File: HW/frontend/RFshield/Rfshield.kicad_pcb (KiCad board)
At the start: 4 copper layers, 73 x 50.9 mm, 148 parts, among them P10 TXENABLE, P11 RXENABLE, P12 XTAL2, P13 GCK1, P14 GCK2, P15 SGPIO_CLK, P16 DA0, P17 DA4, P18 DA7, P19 DD0, P2 VAA, P20 DD5, P21 DD9, P22 RSSI, P23 GND, P24 GND, P25 GND, P26 GND, P27 GND, P28 GND, P29 GND, P3 SCL, P30 GND, P31 GND, P32 GND, P33 XCVR_CLKOUT, P37 INTR, P38 CLKIN, P39 CLKOUT, P4 SDA, P5 SSP1_SCK, P6 SSP1_MOSI, P7 SSP1_MISO, P8 CS_XCVR, P9 CS_AD, Q1 MOSFET_P, T1 RX_BALUN, T2 TX_BALUN, U1 MAX2837, U2 MAX5864, X1 GSG-XTAL4PIN

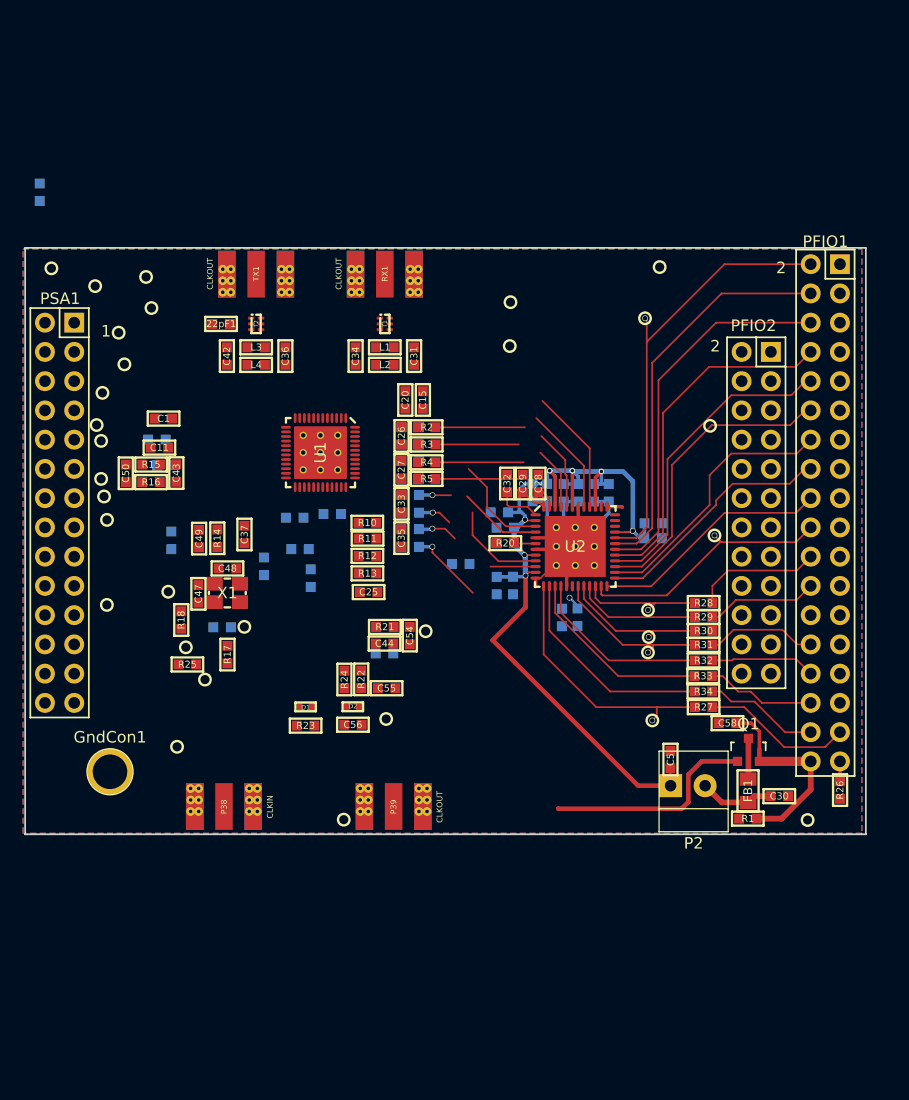
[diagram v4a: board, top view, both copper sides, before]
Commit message: components placed
components placed with reviewed footprints
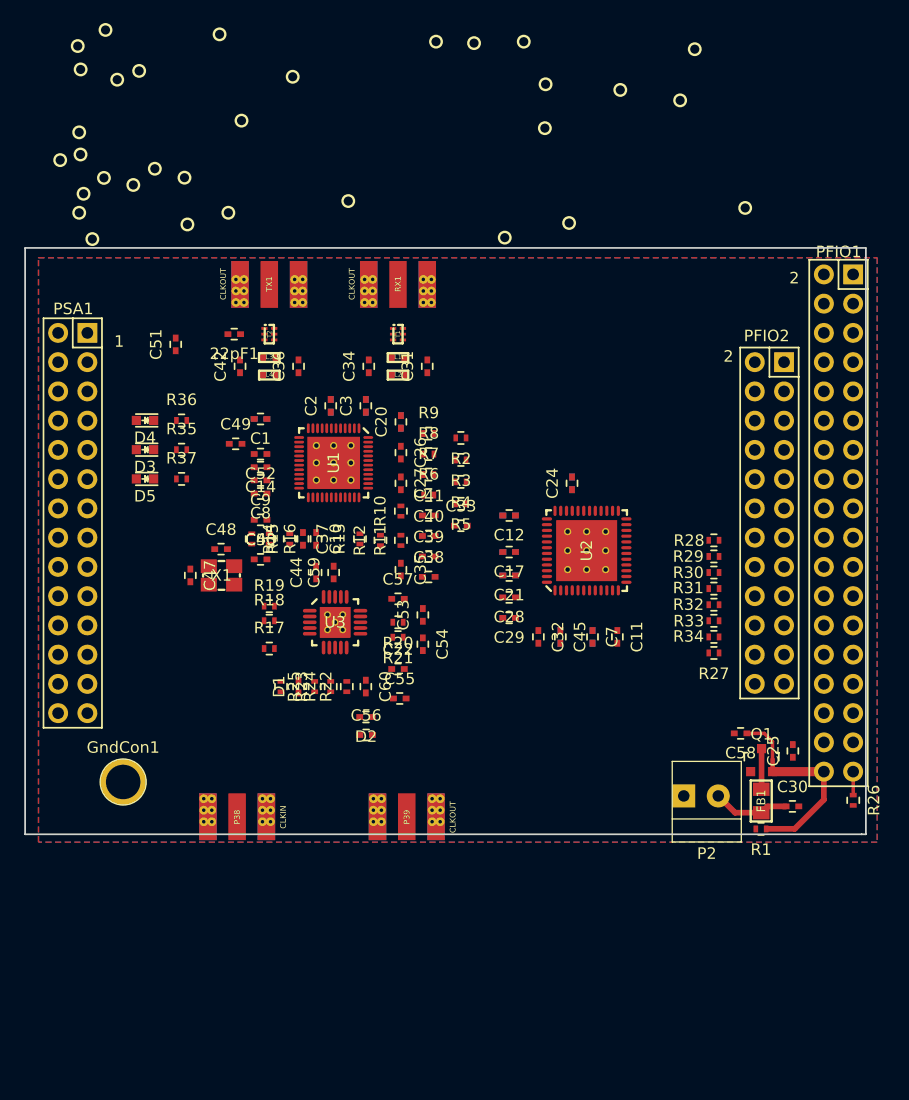
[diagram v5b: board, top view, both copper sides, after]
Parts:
- added C9: 10nF, Capacitors_SMD:C_0402, F.Cu at (39.8, 86.5)
- added D3: LED, LEDs:LED-0603, F.Cu at (29.7, 83.8)
- added D4: LED, LEDs:LED-0603, F.Cu at (29.7, 81.3)
- added D5: LED, LEDs:LED-0603, F.Cu at (29.7, 86.4)
- added R35: 475, Resistors_SMD:R_0402, F.Cu at (32.9, 83.8)
- added R36: 475, Resistors_SMD:R_0402, F.Cu at (32.9, 81.3)
- added R37: 475, Resistors_SMD:R_0402, F.Cu at (32.9, 86.4)
- added U3: SI5351C, hackrf1:GSG-QFN20-4, F.Cu at (46.2, 98.8)
- 22pF1, C1, C11, C13, C16, C18, C19, C20, C23, C25, C26, C27, C28, C29, C30, C31, C32, C33, C34, C35, C36, C37, C4, C42, C43, C44, C46, C47, C48, C49, C50, C54, C55, C56, C58, C6: footprint hackrf1:GSG-0603 -> Capacitors_SMD:C_0402
- C10, C12, C14, C17, C2, C21, C22, C24, C3, C38, C39, C40, C41, C45, C51, C52, C53, C57, C59, C60, C7, C8: footprint hackrf1:GSG-0603 -> Capacitors_SMD:C_0402; moved to F.Cu
- C15, C5: footprint hackrf1:GSG-0603 -> Capacitors_SMD:C_0402; moved to B.Cu
- D1, D2: footprint hackrf1:GSG-0402 -> Capacitors_SMD:C_0402
- L1, L2, L3, L4: footprint hackrf1:GSG-0603 -> hackrf1:GSG-0402
- R1, R10, R11, R12, R13, R14, R15, R16, R17, R18, R2, R20, R21, R22, R23, R24, R25, R26, R27, R28, R29, R3, R30, R31, R32, R33, R34, R4, R5: footprint hackrf1:GSG-0603 -> Resistors_SMD:R_0402
- R19, R6, R7, R8, R9: footprint hackrf1:GSG-0603 -> Resistors_SMD:R_0402; moved to F.Cu
- moved P29 69.0 mm to (36.2, 47.8)
- moved P25 62.6 mm to (26.3, 47.4)
- moved P24 57.0 mm to (61.0, 65.4)
- moved P15 56.4 mm to (42.5, 51.4)
- moved P17 54.1 mm to (62.6, 48.4)
- moved P20 53.8 mm to (58.3, 48.5)
- moved P18 52.7 mm to (55.0, 48.4)
- moved C18 51.4 mm to (61.3, 92.7), turned to 180 degrees
- moved P16 43.8 mm to (66.5, 64.1)
- moved C11 43.0 mm to (70.7, 100.1), turned to 270 degrees
- moved C5 42.6 mm to (45.8, 80.0), turned to 270 degrees
- moved P23 42.0 mm to (24.0, 63.2)
- moved P3 40.6 mm to (24.0, 56.3)
- moved P4 40.4 mm to (24.4, 61.6)
- moved P19 39.5 mm to (71.0, 52.6)
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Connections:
- PFIO1 pad 1: Net-(PFIO1-Pad1) -> (no net)
- PFIO1 pad 11: Net-(PFIO1-Pad11) -> (no net)
- PFIO1 pad 13: Net-(PFIO1-Pad13) -> (no net)
- PFIO1 pad 15: Net-(PFIO1-Pad15) -> (no net)
- PFIO1 pad 17: Net-(PFIO1-Pad17) -> (no net)
- PFIO1 pad 19: Net-(PFIO1-Pad19) -> (no net)
- PFIO1 pad 21: Net-(PFIO1-Pad21) -> (no net)
- PFIO1 pad 23: Net-(PFIO1-Pad23) -> (no net)
- PFIO1 pad 25: Net-(PFIO1-Pad25) -> (no net)
- PFIO1 pad 27: Net-(PFIO1-Pad27) -> (no net)
- PFIO1 pad 29: Net-(PFIO1-Pad29) -> (no net)
- PFIO1 pad 3: Net-(PFIO1-Pad3) -> (no net)
- PFIO1 pad 31: Net-(PFIO1-Pad31) -> (no net)
- PFIO1 pad 5: Net-(PFIO1-Pad5) -> (no net)
- PFIO1 pad 7: Net-(PFIO1-Pad7) -> (no net)
- PFIO1 pad 9: Net-(PFIO1-Pad9) -> (no net)
- PFIO2 pad 1: Net-(PFIO2-Pad1) -> (no net)
- PFIO2 pad 10: Net-(PFIO2-Pad10) -> (no net)
- PFIO2 pad 11: Net-(PFIO2-Pad11) -> (no net)
- PFIO2 pad 12: Net-(PFIO2-Pad12) -> (no net)
- PFIO2 pad 13: Net-(PFIO2-Pad13) -> (no net)
- PFIO2 pad 14: Net-(PFIO2-Pad14) -> (no net)
- PFIO2 pad 15: Net-(PFIO2-Pad15) -> (no net)
- PFIO2 pad 16: Net-(PFIO2-Pad16) -> CLK6
- PFIO2 pad 17: Net-(PFIO2-Pad17) -> (no net)
- PFIO2 pad 19: Net-(PFIO2-Pad19) -> (no net)
- PFIO2 pad 2: Net-(PFIO2-Pad2) -> (no net)
- PFIO2 pad 21: Net-(PFIO2-Pad21) -> (no net)
- PFIO2 pad 23: Net-(PFIO2-Pad23) -> (no net)
- PFIO2 pad 3: Net-(PFIO2-Pad3) -> (no net)
- PFIO2 pad 4: Net-(PFIO2-Pad4) -> (no net)
- PFIO2 pad 5: Net-(PFIO2-Pad5) -> (no net)
- PFIO2 pad 6: Net-(PFIO2-Pad6) -> (no net)
- PFIO2 pad 7: Net-(PFIO2-Pad7) -> (no net)
- PFIO2 pad 8: Net-(PFIO2-Pad8) -> (no net)
- PFIO2 pad 9: Net-(PFIO2-Pad9) -> (no net)
- PSA1 pad 10: Net-(PSA1-Pad10) -> (no net)
- PSA1 pad 13: Net-(PSA1-Pad13) -> (no net)
- PSA1 pad 15: Net-(PSA1-Pad15) -> (no net)
- PSA1 pad 16: Net-(PSA1-Pad16) -> GainCtrl_B7
- PSA1 pad 17: Net-(PSA1-Pad17) -> (no net)
- PSA1 pad 18: Net-(PSA1-Pad18) -> GainCtrl_B6
- PSA1 pad 20: Net-(PSA1-Pad20) -> GainCtrl_B5
- PSA1 pad 22: Net-(PSA1-Pad22) -> GainCtrl_B4
- PSA1 pad 23: Net-(PSA1-Pad23) -> (no net)
- PSA1 pad 24: Net-(PSA1-Pad24) -> GainCtrl_B3
- PSA1 pad 26: Net-(PSA1-Pad26) -> GainCtrl_B2
- PSA1 pad 27: Net-(PSA1-Pad27) -> (no net)
- PSA1 pad 28: Net-(PSA1-Pad28) -> GainCtrl_B1
- PSA1 pad 3: Net-(PSA1-Pad3) -> RXHP
- PSA1 pad 6: Net-(PSA1-Pad6) -> (no net)
- PSA1 pad 8: Net-(PSA1-Pad8) -> (no net)
- U1 pad 12: Net-(U1-Pad12) -> GainCtrl_B1
- U1 pad 14: Net-(U1-Pad14) -> (no net)
- U1 pad 16: /XCVR_CLKOUT -> (no net)
- U1 pad 18: Net-(U1-Pad18) -> (no net)
- U1 pad 3: Net-(U1-Pad3) -> GainCtrl_B5
- U1 pad 32: RSSI -> (no net)
- U1 pad 33: Net-(U1-Pad33) -> GainCtrl_B7
- U1 pad 34: Net-(U1-Pad34) -> GainCtrl_B6
- U1 pad 40: Net-(U1-Pad40) -> RXHP
- U1 pad 6: Net-(U1-Pad6) -> GainCtrl_B4
- U1 pad 8: Net-(U1-Pad8) -> GainCtrl_B3
- U1 pad 9: Net-(U1-Pad9) -> GainCtrl_B2
- U2 pad 38: Net-(U2-Pad38) -> (no net)
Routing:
- net VAA: track 83.9 -> 0.01 mm, vias 7 -> 0
- net DD9: track 38.4 -> 0.00 mm, vias 1 -> 0
- net GND: track 39.5 -> 3.10 mm
- net DD8: track 34.4 -> 0.00 mm
- net DD7: track 32.9 -> 0.00 mm
- net DD6: track 30.4 -> 0.00 mm
- net DD5: track 27.3 -> 0.46 mm
- net DD4: track 26.3 -> 0.50 mm
- net DD3: track 23.3 -> 0.00 mm
- net DD0: track 22.8 -> 0.00 mm, vias 1 -> 0
- net DA0: track 22.3 -> 0.00 mm, vias 1 -> 0
- net DD1: track 20.9 -> 0.00 mm
- net DD2: track 21.2 -> 0.54 mm
- net DA1: track 18.7 -> 0.00 mm
- net !VAA_ENABLE: track 18.7 -> 0.00 mm
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
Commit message: all components placed and routed
drc check pending
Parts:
- added ?: CONN_01X01, Connect:GSG-HOLE-06mm1, F.Cu at (35.6, 105.1)
- added ?: CONN_01X01, Connect:GSG-HOLE-06mm1, F.Cu at (35.7, 103.3)
- added ?: CONN_01X01, Connect:GSG-HOLE-06mm1, F.Cu at (44.9, 67.9)
- added ?: CONN_01X01, Connect:GSG-HOLE-06mm1, F.Cu at (32.8, 67.9)
- added C2: 22pF, Capacitors_SMD:C_0402, F.Cu at (54.8, 87.6)
- added C4: 10nF, Capacitors_SMD:C_0402, B.Cu at (54.8, 87.6)
- added C61: 10nF, Capacitors_SMD:C_0402, B.Cu at (40.4, 86.9)
- added C62: 10nF, Capacitors_SMD:C_0402, B.Cu at (40.4, 88.1)
- added C63: 10nF, Capacitors_SMD:C_0402, B.Cu at (40.4, 85.6)
- added C64: 10nF, Capacitors_SMD:C_0402, B.Cu at (70.2, 90.4)
- added C65: 10nF, Capacitors_SMD:C_0402, B.Cu at (46.0, 91.7)
- added C66: 10nF, Capacitors_SMD:C_0402, B.Cu at (76.5, 85.2)
- added C67: 22pF, Capacitors_SMD:C_0402, F.Cu at (76.5, 85.2)
- added C68: 10nF, Capacitors_SMD:C_0402, B.Cu at (54.2, 86.2)
- added C69: 22pF, Capacitors_SMD:C_0402, F.Cu at (54.2, 86.2)
- added P1: CONN_01X01, Connect:GSG-HOLE-06mm1, F.Cu at (41.7, 81.3)
- added P1: CONN_01X01, Connect:GSG-HOLE-06mm1, F.Cu at (35.2, 73.9)
- added P1: CONN_01X01, Connect:GSG-HOLE-06mm1, F.Cu at (59.4, 92.9)
- added P1: CONN_01X01, Connect:GSG-HOLE-06mm1, F.Cu at (55.8, 90.4)
- added P1: CONN_01X01, Connect:GSG-HOLE-06mm1, F.Cu at (53.6, 90.4)
- added P1: CONN_01X01, Connect:GSG-HOLE-06mm1, F.Cu at (53.0, 93.5)
- added P1: CONN_01X01, Connect:GSG-HOLE-06mm1, F.Cu at (53.6, 91.7)
- added P1: CONN_01X01, Connect:GSG-HOLE-06mm1, F.Cu at (50.3, 91.0)
- added P1: CONN_01X01, Connect:GSG-HOLE-06mm1, F.Cu at (50.7, 89.2)
- added P1: CONN_01X01, Connect:GSG-HOLE-06mm1, F.Cu at (51.8, 94.7)
- added P1: CONN_01X01, Connect:GSG-HOLE-06mm1, F.Cu at (50.7, 93.7)
- added P1: CONN_01X01, Connect:GSG-HOLE-06mm1, F.Cu at (33.5, 78.3)
- added P1: CONN_01X01, Connect:GSG-HOLE-06mm1, F.Cu at (41.6, 94.1)
- added P1: CONN_01X01, Connect:GSG-HOLE-06mm1, F.Cu at (39.8, 94.1)
- added P1: CONN_01X01, Connect:GSG-HOLE-06mm1, F.Cu at (36.7, 93.9)
- added P1: CONN_01X01, Connect:GSG-HOLE-06mm1, F.Cu at (33.7, 92.9)
- added P1: CONN_01X01, Connect:GSG-HOLE-06mm1, F.Cu at (34.5, 94.1)
- added P1: CONN_01X01, Connect:GSG-HOLE-06mm1, F.Cu at (32.9, 95.9)
- added P1: CONN_01X01, Connect:GSG-HOLE-06mm1, F.Cu at (31.6, 97.1)
- added P1: CONN_01X01, Connect:GSG-HOLE-06mm1, F.Cu at (30.5, 98.2)
- added P1: CONN_01X01, Connect:GSG-HOLE-06mm1, F.Cu at (30.4, 100.3)
- added P1: CONN_01X01, Connect:GSG-HOLE-06mm1, F.Cu at (30.4, 102.9)
- added P1: CONN_01X01, Connect:GSG-HOLE-06mm1, F.Cu at (34.7, 79.6)
- added P1: CONN_01X01, Connect:GSG-HOLE-06mm1, F.Cu at (30.4, 105.1)
- added P1: CONN_01X01, Connect:GSG-HOLE-06mm1, F.Cu at (30.4, 106.9)
- added P1: CONN_01X01, Connect:GSG-HOLE-06mm1, F.Cu at (30.4, 108.7)
- added P1: CONN_01X01, Connect:GSG-HOLE-06mm1, F.Cu at (30.4, 110.2)
- added P1: CONN_01X01, Connect:GSG-HOLE-06mm1, F.Cu at (30.4, 111.8)
- added P1: CONN_01X01, Connect:GSG-HOLE-06mm1, F.Cu at (30.4, 113.9)
- added P1: CONN_01X01, Connect:GSG-HOLE-06mm1, F.Cu at (29.1, 115.1)
- added P1: CONN_01X01, Connect:GSG-HOLE-06mm1, F.Cu at (26.4, 115.1)
- added P1: CONN_01X01, Connect:GSG-HOLE-06mm1, F.Cu at (25.5, 114.2)
- added P1: CONN_01X01, Connect:GSG-HOLE-06mm1, F.Cu at (25.5, 110.3)
- added P1: CONN_01X01, Connect:GSG-HOLE-06mm1, F.Cu at (34.7, 85.4)
- added P1: CONN_01X01, Connect:GSG-HOLE-06mm1, F.Cu at (26.9, 108.3)
- added P1: CONN_01X01, Connect:GSG-HOLE-06mm1, F.Cu at (51.9, 92.5)
- added P1: CONN_01X01, Connect:GSG-HOLE-06mm1, F.Cu at (59.4, 89.2)
- added P1: CONN_01X01, Connect:GSG-HOLE-06mm1, F.Cu at (59.4, 87.4)
- added P1: CONN_01X01, Connect:GSG-HOLE-06mm1, F.Cu at (59.4, 85.6)
- added P1: CONN_01X01, Connect:GSG-HOLE-06mm1, F.Cu at (59.0, 83.8)
- added P1: CONN_01X01, Connect:GSG-HOLE-06mm1, F.Cu at (59.4, 82.2)
- added P1: CONN_01X01, Connect:GSG-HOLE-06mm1, F.Cu at (56.5, 81.1)
- added P1: CONN_01X01, Connect:GSG-HOLE-06mm1, F.Cu at (58.2, 80.9)
- added P1: CONN_01X01, Connect:GSG-HOLE-06mm1, F.Cu at (56.8, 79.7)
- added P1: CONN_01X01, Connect:GSG-HOLE-06mm1, F.Cu at (55.2, 85.7)
- added P1: CONN_01X01, Connect:GSG-HOLE-06mm1, F.Cu at (55.2, 78.0)
- added P1: CONN_01X01, Connect:GSG-HOLE-06mm1, F.Cu at (54.8, 76.3)
- added P1: CONN_01X01, Connect:GSG-HOLE-06mm1, F.Cu at (54.8, 74.4)
- added P1: CONN_01X01, Connect:GSG-HOLE-06mm1, F.Cu at (47.1, 67.9)
- added P1: CONN_01X01, Connect:GSG-HOLE-06mm1, F.Cu at (36.6, 67.9)
- added P1: CONN_01X01, Connect:GSG-HOLE-06mm1, F.Cu at (34.9, 67.9)
- added P1: CONN_01X01, Connect:GSG-HOLE-06mm1, F.Cu at (30.6, 67.9)
- added P1: CONN_01X01, Connect:GSG-HOLE-06mm1, F.Cu at (28.6, 67.9)
- added P1: CONN_01X01, Connect:GSG-HOLE-06mm1, F.Cu at (26.9, 69.5)
- added P1: CONN_01X01, Connect:GSG-HOLE-06mm1, F.Cu at (26.9, 67.9)
- added P1: CONN_01X01, Connect:GSG-HOLE-06mm1, F.Cu at (38.7, 86.2)
- added P1: CONN_01X01, Connect:GSG-HOLE-06mm1, F.Cu at (26.9, 71.4)
- added P1: CONN_01X01, Connect:GSG-HOLE-06mm1, F.Cu at (26.9, 72.8)
- added P1: CONN_01X01, Connect:GSG-HOLE-06mm1, F.Cu at (26.9, 74.2)
- added P1: CONN_01X01, Connect:GSG-HOLE-06mm1, F.Cu at (26.9, 75.5)
- added P1: CONN_01X01, Connect:GSG-HOLE-06mm1, F.Cu at (26.9, 77.0)
- added P1: CONN_01X01, Connect:GSG-HOLE-06mm1, F.Cu at (26.9, 78.2)
- added P1: CONN_01X01, Connect:GSG-HOLE-06mm1, F.Cu at (26.9, 79.5)
- added P1: CONN_01X01, Connect:GSG-HOLE-06mm1, F.Cu at (26.9, 80.5)
- added P1: CONN_01X01, Connect:GSG-HOLE-06mm1, F.Cu at (26.9, 82.9)
- added P1: CONN_01X01, Connect:GSG-HOLE-06mm1, F.Cu at (26.9, 85.4)
- added P1: CONN_01X01, Connect:GSG-HOLE-06mm1, F.Cu at (33.7, 90.7)
- added P1: CONN_01X01, Connect:GSG-HOLE-06mm1, F.Cu at (26.9, 88.3)
- added P1: CONN_01X01, Connect:GSG-HOLE-06mm1, F.Cu at (26.9, 89.4)
- added P1: CONN_01X01, Connect:GSG-HOLE-06mm1, F.Cu at (26.9, 90.6)
- added P1: CONN_01X01, Connect:GSG-HOLE-06mm1, F.Cu at (26.9, 93.1)
- added P1: CONN_01X01, Connect:GSG-HOLE-06mm1, F.Cu at (26.9, 95.9)
- added P1: CONN_01X01, Connect:GSG-HOLE-06mm1, F.Cu at (27.6, 97.0)
- added P1: CONN_01X01, Connect:GSG-HOLE-06mm1, F.Cu at (26.9, 98.0)
- added P1: CONN_01X01, Connect:GSG-HOLE-06mm1, F.Cu at (26.9, 99.3)
- added P1: CONN_01X01, Connect:GSG-HOLE-06mm1, F.Cu at (26.9, 101.5)
- added P1: CONN_01X01, Connect:GSG-HOLE-06mm1, F.Cu at (26.9, 103.3)
- added P1: CONN_01X01, Connect:GSG-HOLE-06mm1, F.Cu at (42.4, 92.4)
- added P1: CONN_01X01, Connect:GSG-HOLE-06mm1, F.Cu at (26.9, 104.8)
- added P1: CONN_01X01, Connect:GSG-HOLE-06mm1, F.Cu at (26.9, 106.2)
- added P1: CONN_01X01, Connect:GSG-HOLE-06mm1, F.Cu at (36.9, 84.8)
- added P1: CONN_01X01, Connect:GSG-HOLE-06mm1, F.Cu at (36.9, 88.5)
- added P1: CONN_01X01, Connect:GSG-HOLE-06mm1, F.Cu at (36.9, 86.9)
- added P1: CONN_01X01, Connect:GSG-HOLE-06mm, F.Cu at (59.4, 90.9)
- added P1: CONN_01X01, Connect:GSG-HOLE-06mm1, F.Cu at (33.7, 73.9)
- added P34: CONN_01X01, Connect:GSG-HOLE-06mm1, F.Cu at (47.1, 97.6)
- added P34: CONN_01X01, Connect:GSG-HOLE-06mm1, F.Cu at (60.6, 100.1)
- added P34: CONN_01X01, Connect:GSG-HOLE-06mm1, F.Cu at (63.1, 97.7)
- added P34: CONN_01X01, Connect:GSG-HOLE-06mm1, F.Cu at (51.5, 105.8)
- added P34: CONN_01X01, Connect:GSG-HOLE-06mm1, F.Cu at (51.4, 107.3)
- added P34: CONN_01X01, Connect:GSG-HOLE-06mm1, F.Cu at (56.0, 104.8)
- added P34: CONN_01X01, Connect:GSG-HOLE-06mm1, F.Cu at (55.6, 108.7)
- added P34: CONN_01X01, Connect:GSG-HOLE-06mm1, F.Cu at (55.6, 110.2)
- added P34: CONN_01X01, Connect:GSG-HOLE-06mm1, F.Cu at (35.6, 110.2)
- added P34: CONN_01X01, Connect:GSG-HOLE-06mm1, F.Cu at (35.6, 108.7)
- added P34: CONN_01X01, Connect:GSG-HOLE-06mm1, F.Cu at (35.6, 106.9)
- added P34: CONN_01X01, Connect:GSG-HOLE-06mm1, F.Cu at (76.3, 77.5)
- added P34: CONN_01X01, Connect:GSG-HOLE-06mm1, F.Cu at (61.2, 85.3)
- added P34: CONN_01X01, Connect:GSG-HOLE-06mm1, F.Cu at (61.0, 87.1)
- added P34: CONN_01X01, Connect:GSG-HOLE-06mm1, F.Cu at (69.2, 91.5)
- added P34: CONN_01X01, Connect:GSG-HOLE-06mm1, F.Cu at (65.7, 92.2)
- added P34: CONN_01X01, Connect:GSG-HOLE-06mm1, F.Cu at (61.8, 92.9)
- added P34: CONN_01X01, Connect:GSG-HOLE-06mm1, F.Cu at (61.8, 94.4)
- added P34: CONN_01X01, Connect:GSG-HOLE-06mm1, F.Cu at (61.8, 96.1)
- added P34: CONN_01X01, Connect:GSG-HOLE-06mm1, F.Cu at (60.8, 97.7)
- added P34: CONN_01X01, Connect:GSG-HOLE-06mm1, F.Cu at (58.0, 100.1)
- added P34: CONN_01X01, Connect:GSG-HOLE-06mm1, F.Cu at (55.9, 100.1)
- added P34: CONN_01X01, Connect:GSG-HOLE-06mm1, F.Cu at (64.6, 78.5)
- added P34: CONN_01X01, Connect:GSG-HOLE-06mm1, F.Cu at (51.4, 100.6)
- added P34: CONN_01X01, Connect:GSG-HOLE-06mm1, F.Cu at (45.1, 97.5)
- added P34: CONN_01X01, Connect:GSG-HOLE-06mm1, F.Cu at (37.3, 97.5)
- added P34: CONN_01X01, Connect:GSG-HOLE-06mm1, F.Cu at (35.7, 99.1)
- added P34: CONN_01X01, Connect:GSG-HOLE-06mm1, F.Cu at (35.7, 111.9)
- added P34: CONN_01X01, Connect:GSG-HOLE-06mm1, F.Cu at (46.1, 117.5)
- added P34: CONN_01X01, Connect:GSG-HOLE-06mm1, F.Cu at (43.8, 117.5)
- added P34: CONN_01X01, Connect:GSG-HOLE-06mm1, F.Cu at (41.7, 117.5)
- added P34: CONN_01X01, Connect:GSG-HOLE-06mm1, F.Cu at (48.5, 117.5)
- added P34: CONN_01X01, Connect:GSG-HOLE-06mm1, F.Cu at (55.6, 112.0)
- added P34: CONN_01X01, Connect:GSG-HOLE-06mm1, F.Cu at (63.9, 91.5)
- added P34: CONN_01X01, Connect:GSG-HOLE-06mm1, F.Cu at (55.6, 107.3)
- added P34: CONN_01X01, Connect:GSG-HOLE-06mm1, F.Cu at (57.8, 102.9)
- added P34: CONN_01X01, Connect:GSG-HOLE-06mm1, F.Cu at (66.5, 94.5)
- added P34: CONN_01X01, Connect:GSG-HOLE-06mm1, F.Cu at (75.5, 94.3)
- added P34: CONN_01X01, Connect:GSG-HOLE-06mm1, F.Cu at (77.8, 92.0)
- added P34: CONN_01X01, Connect:GSG-HOLE-06mm1, F.Cu at (77.8, 90.3)
- added P34: CONN_01X01, Connect:GSG-HOLE-06mm1, F.Cu at (77.8, 88.9)
- added P34: CONN_01X01, Connect:GSG-HOLE-06mm1, F.Cu at (77.8, 87.4)
- added P34: CONN_01X01, Connect:GSG-HOLE-06mm1, F.Cu at (77.8, 86.2)
- added P34: CONN_01X01, Connect:GSG-HOLE-06mm1, F.Cu at (77.8, 84.5)
- added P34: CONN_01X01, Connect:GSG-HOLE-06mm1, F.Cu at (76.7, 93.1)
- added P34: CONN_01X01, Connect:GSG-HOLE-06mm1, F.Cu at (77.8, 83.1)
- added P34: CONN_01X01, Connect:GSG-HOLE-06mm1, F.Cu at (77.8, 81.6)
- added P34: CONN_01X01, Connect:GSG-HOLE-06mm1, F.Cu at (77.1, 78.2)
- added P34: CONN_01X01, Connect:GSG-HOLE-06mm1, F.Cu at (71.2, 75.7)
- added P34: CONN_01X01, Connect:GSG-HOLE-06mm1, F.Cu at (69.5, 75.8)
- added P34: CONN_01X01, Connect:GSG-HOLE-06mm1, F.Cu at (67.3, 75.8)
- added P34: CONN_01X01, Connect:GSG-HOLE-06mm1, F.Cu at (66.0, 77.1)
- added P34: CONN_01X01, Connect:GSG-HOLE-06mm1, F.Cu at (63.8, 79.2)
- added P34: CONN_01X01, Connect:GSG-HOLE-06mm1, F.Cu at (62.3, 80.8)
- added P34: CONN_01X01, Connect:GSG-HOLE-06mm1, F.Cu at (61.0, 91.4)
- added P34: CONN_01X01, Connect:GSG-HOLE-06mm1, F.Cu at (73.1, 94.3)
- added P34: CONN_01X01, Connect:GSG-HOLE-06mm1, F.Cu at (61.0, 90.1)
- added P34: CONN_01X01, Connect:GSG-HOLE-06mm1, F.Cu at (61.0, 88.7)
- added P34: CONN_01X01, Connect:GSG-HOLE-06mm1, F.Cu at (71.0, 94.3)
- added P34: CONN_01X01, Connect:GSG-HOLE-06mm1, F.Cu at (69.2, 94.3)
- added P34: CONN_01X01, Connect:GSG-HOLE-06mm1, F.Cu at (59.2, 101.5)
- added R38: 0, Resistors_SMD:R_0402, F.Cu at (33.4, 109.5)
- C11, C8, C9: value 10nF -> 22pF
- C14, C7: value 100nF -> 22pF
- moved P25 98.5 mm to (71.9, 134.6)
- moved P22 95.5 mm to (75.4, 131.4)
- moved P29 95.4 mm to (70.0, 137.0)
- moved P8 92.4 mm to (68.4, 129.7)
- moved P12 91.4 mm to (70.8, 132.1)
- moved P20 90.2 mm to (71.9, 137.7)
- moved P3 90.0 mm to (75.8, 129.9)
- moved P18 89.5 mm to (63.4, 137.4)
- moved P28 87.9 mm to (78.4, 127.4)
- moved P17 87.5 mm to (63.4, 135.9)
- moved P10 87.4 mm to (71.5, 127.4)
- moved P30 87.3 mm to (74.0, 129.0)
- moved P23 87.2 mm to (71.9, 136.2)
- moved P32 86.3 mm to (75.8, 132.9)
- moved P4 84.9 mm to (67.6, 134.6)
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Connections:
- net Net-(C31-Pad1) renamed /RXRF+
- net Net-(C34-Pad1) renamed /RXRF-
- net Net-(C36-Pad1) renamed /TXRF+
- net Net-(C42-Pad1) renamed /TXRF-
- C11 pad 2: GND -> 0V_dig
- C12 pad 2: GND -> 0V_dig
- C13 pad 2: GND -> 0V_dig
- C16 pad 2: GND -> 0V_dig
- C17 pad 2: GND -> 0V_dig
- C18 pad 2: GND -> 0V_dig
- C19 pad 2: GND -> 0V_dig
- C21 pad 2: GND -> 0V_dig
- C22 pad 2: GND -> 0V_dig
- C23 pad 2: GND -> 0V_dig
- C24 pad 2: GND -> 0V_dig
- C28 pad 2: GND -> 0V_dig
- C29 pad 2: GND -> 0V_dig
- C32 pad 2: GND -> 0V_dig
- C44 pad 2: GND -> 0V_dig
- C45 pad 2: GND -> 0V_dig
- C46 pad 2: GND -> 0V_dig
- C47 pad 1: GND -> 0V_dig
- C48 pad 1: GND -> 0V_dig
- C53 pad 2: GND -> 0V_dig
- C54 pad 2: GND -> 0V_dig
- C55 pad 2: GND -> 0V_dig
- C56 pad 2: GND -> 0V_dig
- C57 pad 2: GND -> 0V_dig
- C58 pad 2: GND -> 0V_dig
- C59 pad 2: GND -> 0V_dig
- C60 pad 2: GND -> 0V_dig
- C7 pad 2: GND -> 0V_dig
- D1 pad 1: GND -> 0V_dig
- D2 pad 1: GND -> 0V_dig
- P38 pad 2: GND -> 0V_dig
- P39 pad 2: GND -> 0V_dig
- PFIO1 pad 1: (no net) -> DD9
- PFIO1 pad 10: DD5 -> DD1
- PFIO1 pad 12: DD4 -> Net-(PFIO1-Pad12)
- PFIO1 pad 13: (no net) -> DD0
- PFIO1 pad 14: DD3 -> Net-(PFIO1-Pad14)
- PFIO1 pad 15: (no net) -> Net-(PFIO1-Pad15)
- PFIO1 pad 16: DD2 -> Net-(PFIO1-Pad16)
- PFIO1 pad 17: (no net) -> Net-(PFIO1-Pad17)
- PFIO1 pad 18: DD1 -> Net-(PFIO1-Pad18)
- PFIO1 pad 19: (no net) -> Net-(PFIO1-Pad19)
- PFIO1 pad 2: DD9 -> DD8
- PFIO1 pad 20: DD0 -> (no net)
- PFIO1 pad 21: (no net) -> Net-(PFIO1-Pad21)
- PFIO1 pad 22: Net-(PFIO1-Pad22) -> (no net)
- PFIO1 pad 24: Net-(PFIO1-Pad24) -> (no net)
- PFIO1 pad 26: Net-(PFIO1-Pad26) -> (no net)
- PFIO1 pad 28: Net-(PFIO1-Pad28) -> (no net)
- PFIO1 pad 3: (no net) -> DD7
- PFIO1 pad 30: Net-(PFIO1-Pad30) -> (no net)
- PFIO1 pad 32: Net-(PFIO1-Pad32) -> (no net)
- PFIO1 pad 33: Net-(PFIO1-Pad33) -> (no net)
- PFIO1 pad 34: Net-(PFIO1-Pad34) -> (no net)
- PFIO1 pad 4: DD8 -> DD6
- PFIO1 pad 5: (no net) -> DD5
- PFIO1 pad 6: DD7 -> DD4
- PFIO1 pad 7: (no net) -> DD3
- PFIO1 pad 8: DD6 -> DD2
- R23 pad 2: GND -> 0V_dig
- R27 pad 1: Net-(PFIO1-Pad33) -> Net-(PFIO1-Pad21)
- R28 pad 2: Net-(PFIO1-Pad22) -> Net-(PFIO1-Pad12)
- R29 pad 2: Net-(PFIO1-Pad24) -> Net-(PFIO1-Pad15)
- R30 pad 2: Net-(PFIO1-Pad26) -> Net-(PFIO1-Pad14)
- R31 pad 2: Net-(PFIO1-Pad28) -> Net-(PFIO1-Pad17)
- R32 pad 2: Net-(PFIO1-Pad30) -> Net-(PFIO1-Pad16)
- R33 pad 2: Net-(PFIO1-Pad32) -> Net-(PFIO1-Pad19)
- R34 pad 2: Net-(PFIO1-Pad34) -> Net-(PFIO1-Pad18)
- U2 pad 0: GND -> 0V_dig
- U2 pad 12: GND -> 0V_dig
- U2 pad 17: GND -> 0V_dig
- U2 pad 37: GND -> 0V_dig
- U2 pad 42: GND -> 0V_dig
- U2 pad 5: GND -> 0V_dig
- U2 pad 7: GND -> 0V_dig
- U3 pad 0: GND -> 0V_dig
- X1 pad 2: GND -> 0V_dig
- X1 pad 4: GND -> 0V_dig
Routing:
- net VAA: track 0.01 -> 188.6 mm, vias 0 -> 20
- net GND: track 3.10 -> 127.8 mm, vias 0 -> 3
- net VCC: track 17.8 -> 131.5 mm, vias 0 -> 11
- net SSP1_MOSI: track 0.00 -> 98.7 mm, vias 0 -> 4
- net 0V_dig: track 0.00 -> 79.5 mm, vias 0 -> 1
- net RXENABLE: track 0.00 -> 75.2 mm, vias 0 -> 2
- net TXENABLE: track 0.00 -> 75.1 mm, vias 0 -> 2
- net !VAA_ENABLE: track 0.00 -> 73.6 mm, vias 0 -> 3
- net SSP1_SCK: track 0.00 -> 65.9 mm, vias 0 -> 2
- net RXHP: track 0.00 -> 52.1 mm, vias 0 -> 2
- net CS_AD: track 0.00 -> 47.2 mm, vias 0 -> 1
- net OEB: track 0.00 -> 45.3 mm, vias 0 -> 3
- net GainCtrl_B5: track 0.00 -> 43.5 mm, vias 0 -> 2
- net GainCtrl_B2: track 0.00 -> 43.1 mm, vias 0 -> 2
- net GainCtrl_B1: track 0.00 -> 43.1 mm, vias 0 -> 2
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- added copper zone on B.Cu, net 0V_dig
- added copper zone on F.Cu, net 0V_dig
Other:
- outline, holes or cut-outs redrawn
- net class Default: clearance 0.2 -> 0.16
- rule trace_clearance: 0.2 -> 0.16
- rule via_min_size: 0.5 -> 0.4
- board text removed: "1"

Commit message: bom, position files and gerbers generated
again
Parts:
- removed 22pF1: C_Small, Capacitors_SMD:C_0402
- removed P12: XTAL2, hackrf1:GSG-TESTPOINT-30MIL-MASKONLY
- removed P14: GCK2, hackrf1:GSG-TESTPOINT-30MIL-MASKONLY
- removed P15: SGPIO_CLK, hackrf1:GSG-TESTPOINT-30MIL-MASKONLY
- removed P17: DA4, hackrf1:GSG-TESTPOINT-30MIL-MASKONLY
- removed P19: DD0, hackrf1:GSG-TESTPOINT-30MIL-MASKONLY
- removed P20: DD5, hackrf1:GSG-TESTPOINT-30MIL-MASKONLY
- removed P21: DD9, hackrf1:GSG-TESTPOINT-30MIL-MASKONLY
- removed P22: RSSI, hackrf1:GSG-TESTPOINT-30MIL-MASKONLY
- removed P23, P24, P25, P28, P30, P31: GND, hackrf1:GSG-TESTPOINT-30MIL-MASKONLY
- removed P3: SCL, hackrf1:GSG-TESTPOINT-30MIL-MASKONLY
- removed P33: XCVR_CLKOUT, hackrf1:GSG-TESTPOINT-30MIL-MASKONLY
- removed P37: INTR, hackrf1:GSG-TESTPOINT-30MIL-MASKONLY
- removed P4: SDA, hackrf1:GSG-TESTPOINT-30MIL-MASKONLY
- removed P5: SSP1_SCK, hackrf1:GSG-TESTPOINT-30MIL-MASKONLY
- removed P6: SSP1_MOSI, hackrf1:GSG-TESTPOINT-30MIL-MASKONLY
- removed P7: SSP1_MISO, hackrf1:GSG-TESTPOINT-30MIL-MASKONLY
- removed P8: CS_XCVR, hackrf1:GSG-TESTPOINT-30MIL-MASKONLY
- removed P9: CS_AD, hackrf1:GSG-TESTPOINT-30MIL-MASKONLY
- added 0Vdig: GND, Connect:testpoint1mm, F.Cu at (67.4, 96.0)
- added C72: 22pF, Capacitors_SMD:C_0402, F.Cu at (39.0, 72.9)
- added cs_ad: CS_AD, Connect:testpoint1mm, F.Cu at (65.0, 69.8)
- added gck2: GCK2, Connect:testpoint1mm, F.Cu at (71.3, 101.6)
- added gnd: GND, Connect:testpoint1mm, F.Cu at (80.7, 116.1)
- added gnd: GND, Connect:testpoint1mm, F.Cu at (33.0, 105.1)
- added gpioclk: SGPIO_CLK, Connect:testpoint1mm, F.Cu at (82.7, 106.8)
- added miso: SSP1_MISO, Connect:testpoint1mm, F.Cu at (28.5, 73.7)
- added mosi: SSP1_MOSI, Connect:testpoint1mm, F.Cu at (57.6, 69.9)
- added sck: SSP1_SCK, Connect:testpoint1mm, F.Cu at (61.1, 69.8)
- added scl: SCL, Connect:testpoint1mm, F.Cu at (33.0, 97.9)
- added sda: SDA, Connect:testpoint1mm, F.Cu at (33.0, 101.2)
- P10, P11, P13, P16, P18, P26, P27, P29, P32: footprint hackrf1:GSG-TESTPOINT-30MIL-MASKONLY -> Connect:testpoint1mm
- moved P26 81.0 mm to (22.6, 69.2)
- moved P10 63.9 mm to (29.0, 79.7)
- moved P18 63.0 mm to (78.8, 76.3)
- moved P29 62.2 mm to (56.3, 76.3)
- moved P27 52.7 mm to (36.7, 95.9)
- moved P11 52.7 mm to (61.5, 79.5)
- moved P16 45.3 mm to (75.3, 92.4)
- moved P32 38.6 mm to (78.7, 94.4)
- moved P13 34.1 mm to (63.0, 100.7)
- renumbered P34 to ?, P1 to ?, GndCon1 to ?, C4 to C70, C2 to C71
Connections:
- U1 pad 16: (no net) -> /XCVR_CLKOUT
- U1 pad 32: (no net) -> RSSI
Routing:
- net CS_AD: track 47.2 -> 58.2 mm, vias 1 -> 2
- net GND: track 127.8 -> 137.0 mm
- net GCK1: track 23.4 -> 31.2 mm
- net SSP1_SCK: track 65.9 -> 72.5 mm, vias 2 -> 3
- net 0V_dig: track 79.5 -> 83.9 mm
- net SSP1_MISO: track 37.0 -> 40.9 mm
- net SSP1_MOSI: track 98.7 -> 101.6 mm
- net SGPIO_CLK: track 40.3 -> 42.9 mm
